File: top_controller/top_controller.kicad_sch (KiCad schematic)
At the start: 93 parts, among them J1 SWD, J10 OUT3, J11 OUT7, J12 OUT4, J13 OUT8, J2 UART, J3 BOOT0, J4 USB_C_Receptacle_USB2.0, J5 OUT1, J6 OUT5, J7 PIN, J8 OUT2, J9 OUT6, SW1 RESET, U1 STM32F103C8Tx, U2 LT3045xMSE, U3 AD5754BREZ, U4 AD5754BREZ, U5 REF192, U6 EPM78V2, Y1 8MHz

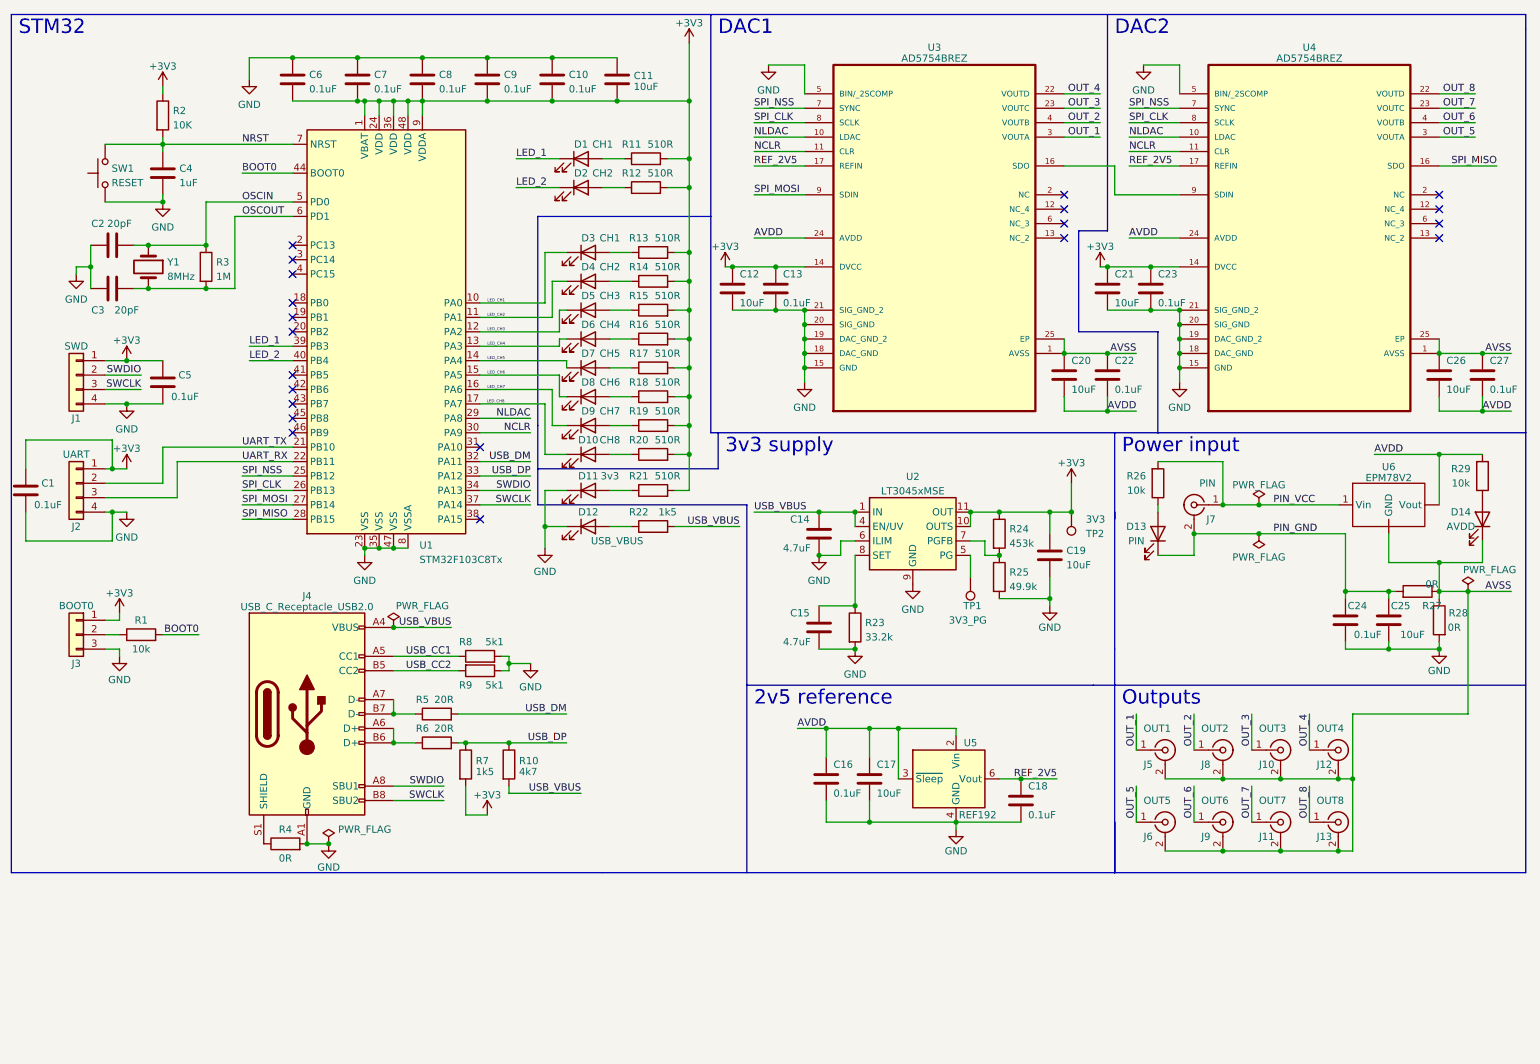
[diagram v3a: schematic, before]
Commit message: Assigned footprints
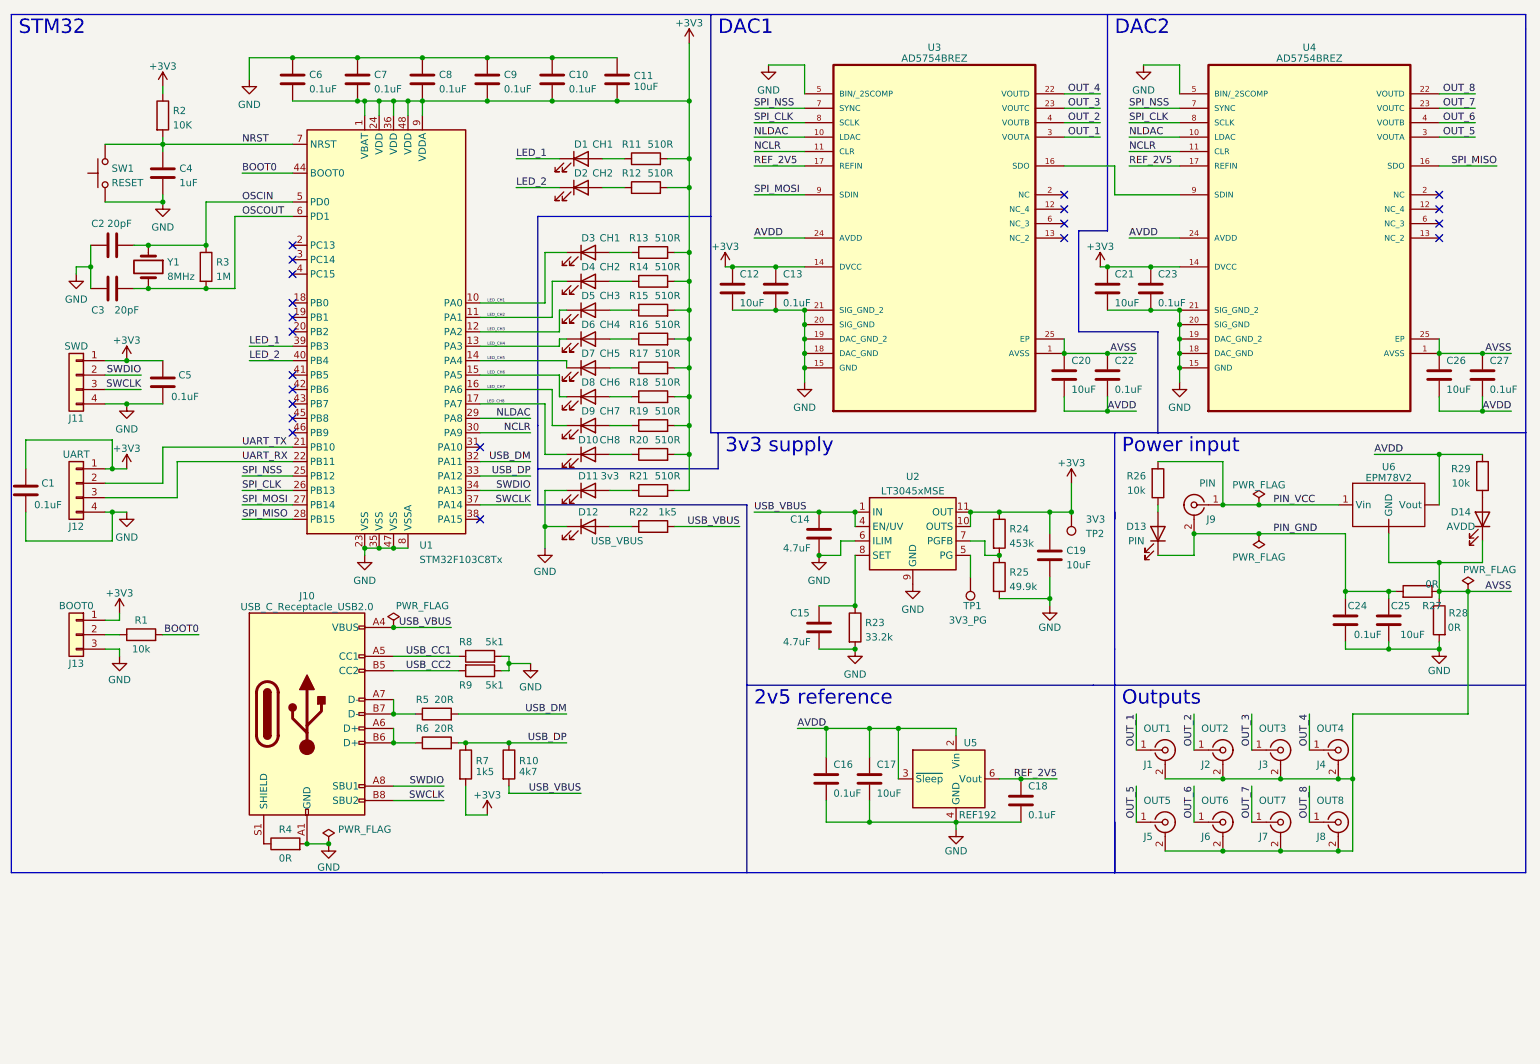
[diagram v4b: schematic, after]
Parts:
- C1, C10, C13, C16, C18, C2, C22, C23, C24, C27, C3, C4, C5, C6, C7, C8, C9: footprint (none) -> Capacitor_SMD:C_0603_1608Metric
- C11, C12, C14, C15, C17, C19, C20, C21, C25, C26: footprint (none) -> Capacitor_SMD:C_1206_3216Metric
- D1, D10, D11, D12, D13, D14, D2, D3, D4, D5, D6, D7, D8, D9: footprint (none) -> LED_SMD:LED_0805_2012Metric
- J1: renamed from J5; footprint (none) -> CONBNC002:CONBNC002
- J10: renamed from J4; footprint (none) -> Connector_USB:USB_C_Receptacle_GCT_USB4105-xx-A_16P_TopMnt_Horizontal
- J11: renamed from J1; footprint (none) -> Connector_PinHeader_2.54mm:PinHeader_1x04_P2.54mm_Vertical
- J12: renamed from J2; footprint (none) -> Connector_PinHeader_2.54mm:PinHeader_1x04_P2.54mm_Vertical
- J13: renamed from J3; footprint (none) -> Connector_PinHeader_2.54mm:PinHeader_1x03_P2.54mm_Vertical
- J2: renamed from J8; footprint (none) -> CONBNC002:CONBNC002
- J3: renamed from J10; footprint (none) -> CONBNC002:CONBNC002
- J4: renamed from J12; footprint (none) -> CONBNC002:CONBNC002
- J5: renamed from J6; footprint (none) -> CONBNC002:CONBNC002
- J6: renamed from J9; footprint (none) -> CONBNC002:CONBNC002
- J7: renamed from J11; footprint (none) -> CONBNC002:CONBNC002
- J8: renamed from J13; footprint (none) -> CONBNC002:CONBNC002
- J9: renamed from J7; footprint (none) -> CONBNC002:CONBNC002
- R1, R10, R11, R12, R13, R14, R15, R16, R17, R18, R19, R2, R20, R21, R22, R23, R25, R26, R27, R28, R29, R4, R5, R6, R7, R8, R9: footprint (none) -> Resistor_SMD:R_0603_1608Metric
- R24: footprint (none) -> Resistor_SMD:R_0805_2012Metric
- R3: footprint (none) -> Resistor_SMD:R_2512_6332Metric
- SW1: footprint (none) -> TS04-66:SW_TS04-66-95-BK-100-SMT
- U3, U4: footprint SOP65P640X120-25N -> AD5754BREZ:SOP65P640X120-25N
- U5: footprint (none) -> Package_SO:SOIC-8_3.9x4.9mm_P1.27mm
- Y1: footprint (none) -> Crystal:Crystal_SMD_HC49-SD

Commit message: Added testpoints
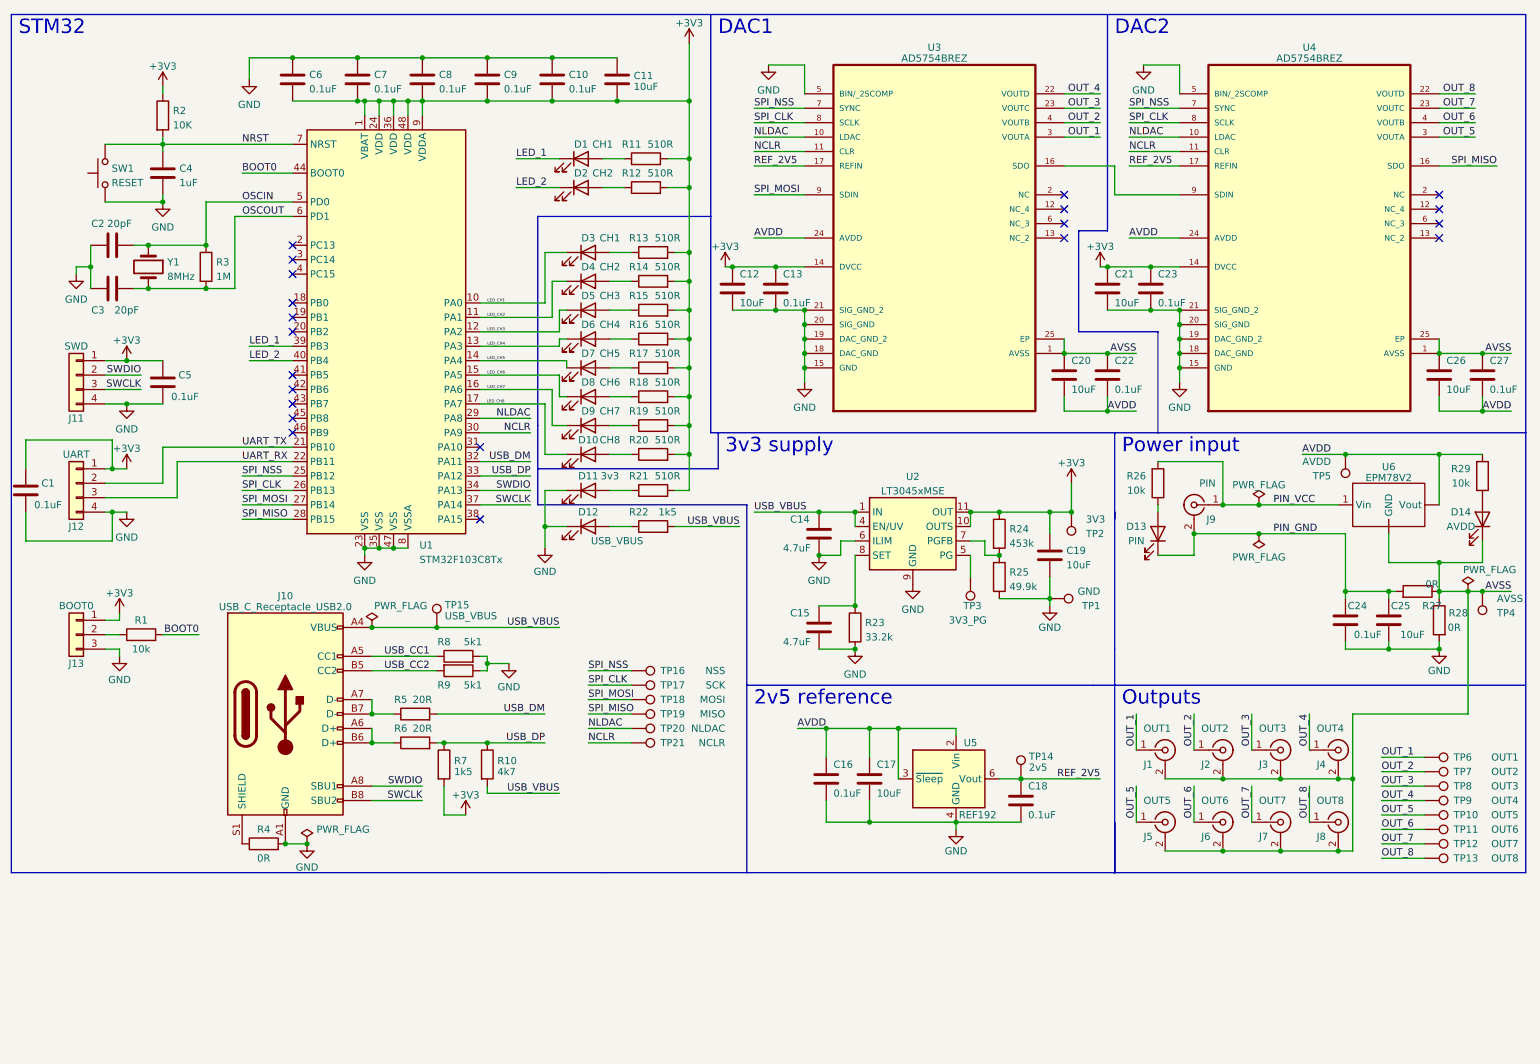
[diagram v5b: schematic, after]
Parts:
- added TP1: GND, TestPoint:TestPoint_Keystone_5010-5014_Multipurpose, symbol Connector:TestPoint
- added TP10: OUT5, TestPoint:TestPoint_Keystone_5010-5014_Multipurpose, symbol Connector:TestPoint
- added TP11: OUT6, TestPoint:TestPoint_Keystone_5010-5014_Multipurpose, symbol Connector:TestPoint
- added TP12: OUT7, TestPoint:TestPoint_Keystone_5010-5014_Multipurpose, symbol Connector:TestPoint
- added TP13: OUT8, TestPoint:TestPoint_Keystone_5010-5014_Multipurpose, symbol Connector:TestPoint
- added TP14: 2v5, TestPoint:TestPoint_Keystone_5010-5014_Multipurpose, symbol Connector:TestPoint
- added TP15: USB_VBUS, TestPoint:TestPoint_Keystone_5010-5014_Multipurpose, symbol Connector:TestPoint
- added TP16: NSS, TestPoint:TestPoint_Keystone_5010-5014_Multipurpose, symbol Connector:TestPoint
- added TP17: SCK, TestPoint:TestPoint_Keystone_5010-5014_Multipurpose, symbol Connector:TestPoint
- added TP18: MOSI, TestPoint:TestPoint_Keystone_5010-5014_Multipurpose, symbol Connector:TestPoint
- added TP19: MISO, TestPoint:TestPoint_Keystone_5010-5014_Multipurpose, symbol Connector:TestPoint
- added TP20: NLDAC, TestPoint:TestPoint_Keystone_5010-5014_Multipurpose, symbol Connector:TestPoint
- added TP21: NCLR, TestPoint:TestPoint_Keystone_5010-5014_Multipurpose, symbol Connector:TestPoint
- added TP4: AVSS, TestPoint:TestPoint_Keystone_5010-5014_Multipurpose, symbol Connector:TestPoint
- added TP5: AVDD, TestPoint:TestPoint_Keystone_5010-5014_Multipurpose, symbol Connector:TestPoint
- added TP6: OUT1, TestPoint:TestPoint_Keystone_5010-5014_Multipurpose, symbol Connector:TestPoint
- added TP7: OUT2, TestPoint:TestPoint_Keystone_5010-5014_Multipurpose, symbol Connector:TestPoint
- added TP8: OUT3, TestPoint:TestPoint_Keystone_5010-5014_Multipurpose, symbol Connector:TestPoint
- added TP9: OUT4, TestPoint:TestPoint_Keystone_5010-5014_Multipurpose, symbol Connector:TestPoint
- TP2: footprint (none) -> TestPoint:TestPoint_Keystone_5010-5014_Multipurpose
- TP3: renamed from TP1; footprint (none) -> TestPoint:TestPoint_Keystone_5010-5014_Multipurpose
- U6: footprint (none) -> EPM78V2:EPM78V2
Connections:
- net AVDD: now also TP5.1
- net AVSS: now also TP4.1
- net GND: now also TP1.1
- net NCLR: now also TP21.1
- net NLDAC: now also TP20.1
- net OUT_1: now also TP6.1
- net OUT_2: now also TP7.1
- net OUT_3: now also TP8.1
- net OUT_4: now also TP9.1
- net OUT_5: now also TP10.1
- net OUT_6: now also TP11.1
- net OUT_7: now also TP12.1
- net OUT_8: now also TP13.1
- net REF_2V5: now also TP14.1
- net SPI_CLK: now also TP17.1
- net SPI_MISO: now also TP19.1
- net SPI_MOSI: now also TP18.1
- net SPI_NSS: now also TP16.1
- net USB_VBUS: now also TP15.1
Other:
- moved on the sheet: J10, R10, R4, R5, R6, R7, R8, R9
